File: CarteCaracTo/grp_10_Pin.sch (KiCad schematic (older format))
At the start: 1 part, among them J1 Conn_02x10_Counter_Clockwise

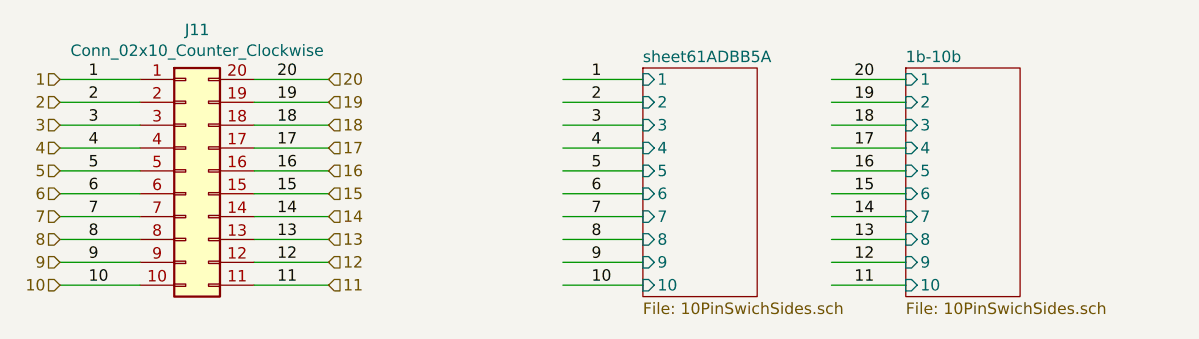
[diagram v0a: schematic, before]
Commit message: Mise en forme de la carte + version carte ASIC et Carac separées
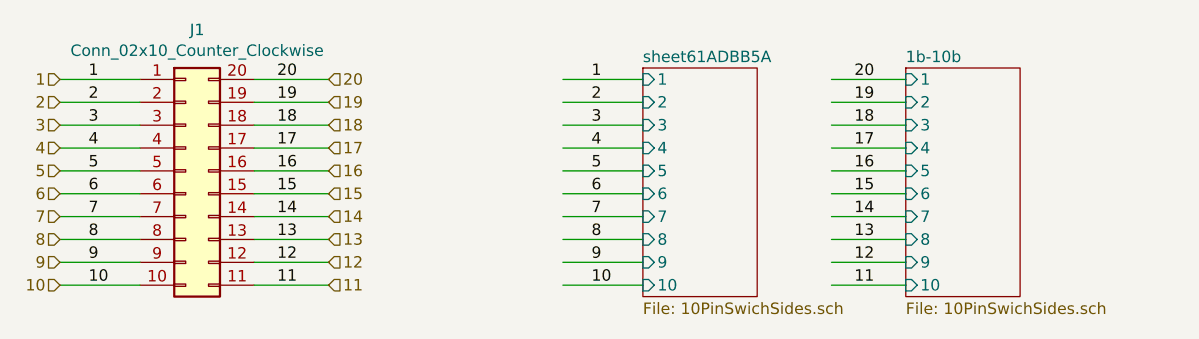
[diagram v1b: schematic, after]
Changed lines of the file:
@@
 $Descr A4 11693 8268
 encoding utf-8
-Sheet 71 123
+Sheet 48 123
 Title ""
 Date ""
@@
 AR Path="/61533310/5E6A9E8D" Ref="J31"  Part="1"
 AR Path="/615B5DD5/5E6A9E8D" Ref="J41"  Part="1"
-F 0 "J11" H 2850 3392 50  0000 C CNN
+F 0 "J1" H 2850 3392 50  0000 C CNN
 F 1 "Conn_02x10_Counter_Clockwise" H 2850 3301 50  0000 C CNN
 F 2 "Button_Switch_THT:SW_DIP_SPSTx10_Slide_9.78x27.58mm_W7.62mm_P2.54mm" H 2800 2775 50  0001 C CNN

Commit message: ID des pins, option capa sur sortie, option GND ou plan de masse sur BNC
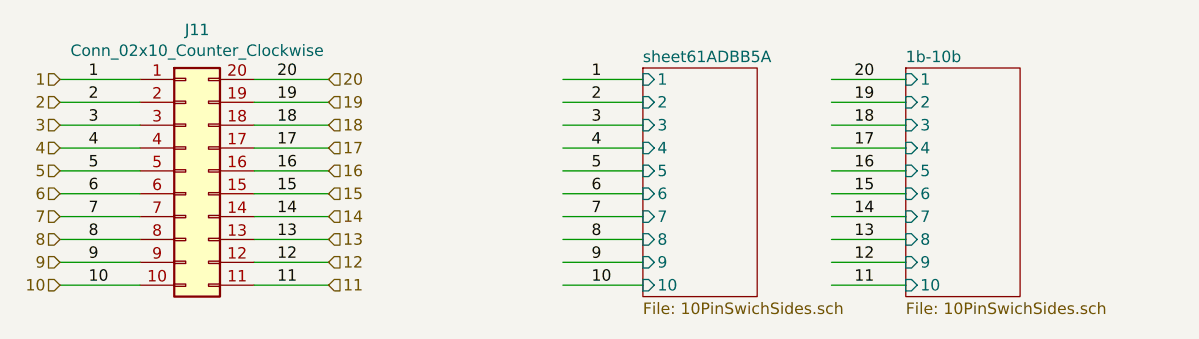
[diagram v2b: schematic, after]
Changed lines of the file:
@@
 $Descr A4 11693 8268
 encoding utf-8
-Sheet 48 123
+Sheet 71 123
 Title ""
 Date ""
@@
 AR Path="/61533310/5E6A9E8D" Ref="J31"  Part="1"
 AR Path="/615B5DD5/5E6A9E8D" Ref="J41"  Part="1"
-F 0 "J1" H 2850 3392 50  0000 C CNN
+F 0 "J11" H 2850 3392 50  0000 C CNN
 F 1 "Conn_02x10_Counter_Clockwise" H 2850 3301 50  0000 C CNN
 F 2 "Button_Switch_THT:SW_DIP_SPSTx10_Slide_9.78x27.58mm_W7.62mm_P2.54mm" H 2800 2775 50  0001 C CNN
